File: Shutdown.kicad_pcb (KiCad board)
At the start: 4 copper layers, 93.5 x 70 mm, 218 parts, among them IC1 MCP1804T-C002I/OT, J1 DRC23-24PA, J2 0430450629, Q1 SI2347DS-T1-GE3, Q10 SI2318CDS-T1-GE3, Q11 SI2347DS-T1-GE3, Q12 SI2347DS-T1-GE3, Q13 SI2347DS-T1-GE3, Q14 MMBT3904L RFG, Q15 SI2347DS-T1-GE3, Q16 SI2347DS-T1-GE3, Q17 MMBT3904L RFG, Q18 SI2318CDS-T1-GE3, Q19 SI2318CDS-T1-GE3, Q2 SI2347DS-T1-GE3, Q20 SI2347DS-T1-GE3, Q21 SI2347DS-T1-GE3, Q22 SI2347DS-T1-GE3, Q23 SI2318CDS-T1-GE3, Q3 SI2318CDS-T1-GE3, Q4 SI2347DS-T1-GE3, Q5 SI2318CDS-T1-GE3, Q6 SI2347DS-T1-GE3, Q7 SI2347DS-T1-GE3, Q8 SI2347DS-T1-GE3, Q9 SI2318CDS-T1-GE3, U1 LM393BIDR, U2 LM393BIDR, U4 LM393BIDR, U5 CD4002BM96, U6 LM393BIDR

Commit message: test push
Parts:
- removed ? (x4): , 
- removed J1: DRC23-24PA, -Connectors:DRC2324PB
- removed J2: 0430450629, -Connectors:CONN_SD-43045-010_06_MOL
- removed R95: 100k, Resistor_SMD:R_0603_1608Metric_Pad0.98x0.95mm_HandSolder
- added C12: 100nF, Capacitor_SMD:C_0603_1608Metric_Pad1.08x0.95mm_HandSolder, F.Cu at (345.9, 132.9)
- added C13: 100nF, Capacitor_SMD:C_0603_1608Metric_Pad1.08x0.95mm_HandSolder, F.Cu at (345.9, 135.4)
- added J3: 348302001, -Connectors:348302001, F.Cu at (170.4, 188.4)
- added J4: 348300801, -Connectors:348300801, F.Cu at (227.0, 188.4)
- added R60: 510, Resistor_SMD:R_0603_1608Metric_Pad0.98x0.95mm_HandSolder, F.Cu at (387.2, 131.2)
- added U3: LM393BIDR, Package_SO:SOIC-8_3.9x4.9mm_P1.27mm, F.Cu at (395.4, 55.1)
- added U7: TSB712AIDT, Package_SO:SOIC-8_5.3x5.3mm_P1.27mm, F.Cu at (338.6, 142.0)
- C1: value 470nF -> 10uF
- C2: value 100nF -> 10uF
- C3: value 1uF -> 470nF
- C4, C5: value 100nF -> 1uF
- C8: value 1uF -> 100nF
- D1, D10, D11, D12, D28, D6, D7, D8: value Red -> BZT52C16; footprint LED_SMD:LED_0805_2012Metric -> Diode_SMD:D_SOD-123
- D13, D19, D2, D21, D23, D3, D4, D41, D42, D45, D5: value BZT52C16 -> Red; footprint Diode_SMD:D_SOD-123 -> LED_SMD:LED_0805_2012Metric
- D17: value BZT52C16 -> Red; footprint Diode_SMD:D_SOD-123 -> LED_SMD:LED_0805_2012Metric; moved to F.Cu
- D27, D32, D33, D35, D36, D38, D39, D44, Q20, R64, R66, R70, R72, R93, TP17, TP20, TP21, TP22, TP23, TP25: moved to F.Cu
- D30, D31, D34, D37: value Red -> BZT52C16; footprint LED_SMD:LED_0805_2012Metric -> Diode_SMD:D_SOD-123; moved to F.Cu
- Q10: value SI2318CDS-T1-GE3 -> MMBT3904L RFG
- Q11: value SI2347DS-T1-GE3 -> MMBT3904L RFG
- Q13, Q15, Q2, Q7: value SI2347DS-T1-GE3 -> SI2318CDS-T1-GE3
- Q14: value MMBT3904L RFG -> SI2347DS-T1-GE3
- Q17: value MMBT3904L RFG -> SI2318CDS-T1-GE3
- Q18, Q19, Q23, Q9: value SI2318CDS-T1-GE3 -> SI2347DS-T1-GE3
- R1, R37, R38, R39: value 100k -> 10k
- R11: value 100k -> 2.2k
- R12: value 10k -> 100k; moved to F.Cu
- R13, R18, R30, R52: value 510 -> 100k
- R17: value 100k -> 390k
- R21, R22, R26, R27, R28, R3: value 100k -> 0
- R23, R25: value 510 -> 0
- R24: value 10k -> 0
- R29: value 10k -> 100k
- R31: value 1k -> 100k
- R32: value 2.2k -> 100k
- R35: value 100k -> 1k
- R36: value 0 -> 1k
- R4, R5, R58, R6, R77, R78, R81, R82, R94: value 100k -> 510
- R40, R41, R42: value 510 -> 10k
- R43: value 1k -> 3M
- R44: value 10k -> 30k
- R45: value 10k -> 120k
- R47: value 510 -> 3k
- R53, R54: value 10k -> 510
- R55: value 3k -> 100k
- R56: value 3M -> 100k
- R57, R63, R67, R68, R69: value 510 -> 100k; moved to F.Cu
- R59: value 100k -> 51
- R61: value 120k -> 100k
- R62: value 30k -> 100k
- R65, R71: value 510 -> 51; moved to F.Cu
- R7: value 390k -> 510
- R73, R74, R75: value 51 -> 100k
- R80: value 100k -> 1M
- R84, R87, R88, R91, R92: value 0 -> 100k; moved to F.Cu
- R85: value 100k -> 510; moved to F.Cu
- R86: value 0 -> 510
- R89, R90: value 0 -> 510; moved to F.Cu
- TP24: footprint TestPoint:TestPoint_Pad_1.5x1.5mm -> TestPoint:TestPoint_Pad_1.0x1.0mm; moved to F.Cu
- TP27: footprint TestPoint:TestPoint_Pad_1.5x1.5mm -> TestPoint:TestPoint_Pad_1.0x1.0mm
- TP7, TP8: footprint TestPoint:TestPoint_Pad_1.0x1.0mm -> TestPoint:TestPoint_Pad_1.5x1.5mm
- U6: value LM393BIDR -> TSB712AIDT; footprint Package_SO:SOIC-8_3.9x4.9mm_P1.27mm -> Package_SO:SOIC-8_5.3x5.3mm_P1.27mm
- moved R47 310.6 mm to (419.2, 39.8), turned to 0 degrees
- moved R42 308.7 mm to (414.9, 49.9), turned to 0 degrees
- moved D26 304.7 mm to (414.8, 119.1), turned to 0 degrees
- moved R41 301.7 mm to (414.9, 47.4), turned to 0 degrees
- moved D28 301.0 mm to (414.8, 122.5), turned to 0 degrees
- moved TP23 300.0 mm to (408.6, 77.2), turned to 0 degrees
- moved R31 299.9 mm to (410.6, 44.9)
- moved TP22 299.7 mm to (408.6, 73.6), turned to 0 degrees
- moved TP21 299.5 mm to (408.6, 70.0), turned to 0 degrees
- moved Q16 298.6 mm to (409.3, 119.8)
- moved TP6 296.1 mm to (417.0, 79.0)
- moved TP8 295.8 mm to (401.4, 66.5)
- moved R40 294.8 mm to (414.9, 44.9), turned to 0 degrees
- moved D44 294.7 mm to (410.0, 95.1), turned to 0 degrees
- moved R29 292.9 mm to (410.6, 39.8), turned to 0 degrees
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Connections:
- C1 pad 2: Net-(C1-Pad2) -> /ISENSE-EXT
- C10 pad 2: /ACCUM-VOUT -> 12V
- C11 pad 2: Net-(U6A--) -> 12V
- C2 pad 2: 12V -> /BSE
- C3 pad 2: BATT+PROT -> Net-(C3-Pad2)
- C4 pad 2: 12V -> BATT+PROT
- C6 pad 2: 12V -> Net-(U4A--)
- C9 pad 2: /BRAKE-VOUT -> 12V
- D1 pad 1: GND -> Net-(D1-K)
- D10 pad 1: Net-(D10-K) -> /IMD-Fault-Passthru/OUTPUT
- D11 pad 1: GND -> Net-(D11-K)
- D11 pad 2: Net-(D11-A) -> GND
- D12 pad 1: Net-(D12-K) -> 12V
- D13 pad 1: /BMS-Fault-Passthru/OUTPUT -> GND
- D15 pad 1: Net-(D15-K) -> 12V
- D16 pad 1: Net-(D16-K) -> GND
- D17 pad 1: Net-(D17-K) -> GND
- D18 pad 1: Net-(D18-K) -> /BMS-Fault-Passthru/INPUT
- D18 pad 2: GND -> Net-(D18-A)
- D19 pad 1: /IMD-Fault-Passthru/OUTPUT -> Net-(D19-K)
- D2 pad 1: /HVILS-A -> GND
- D20 pad 2: GND -> Net-(D20-A)
- D21 pad 1: BATT+PROT -> Net-(D19-K)
- D22 pad 1: Net-(D22-K) -> BATT+PROT
- D22 pad 2: GND -> Net-(D22-A)
- D23 pad 1: /CS-A -> Net-(D23-K)
- D24 pad 1: /BOTS-A -> Net-(D24-K)
- D25 pad 1: GND -> Net-(D23-K)
- D26 pad 1: /BOTS-B -> /BMS-Fault-Passthru/OUTPUT
- D27 pad 1: /BYPASS -> Net-(D27-K)
- D28 pad 1: GND -> Net-(D28-K)
- D29 pad 1: GND -> Net-(D27-K)
- D3 pad 1: BATT+PROT -> GND
- D30 pad 1: GND -> BATT+PROT
- D31 pad 1: GND -> Net-(D31-K)
- D34 pad 1: GND -> /HVILS-A
- D35 pad 1: Net-(D10-K) -> GND
- D36 pad 1: Net-(D12-K) -> GND
- D37 pad 1: Net-(D16-K) -> /CRASH-SW-A
- D4 pad 1: /BMS-Fault-Passthru/INPUT -> /BYPASS-BTN
- D40 pad 1: 12V -> /BOTS-A
- D41 pad 1: 12V -> GND
- D42 pad 1: Net-(D42-K) -> GND
- D43 pad 1: BATT+PROT -> /BOTS-B
- D45 pad 1: Net-(D45-K) -> GND
- D45 pad 2: GND -> Net-(D45-A)
- D5 pad 1: Net-(D5-K) -> /BYPASS-BTN
- D6 pad 1: /BYPASS -> Net-(D6-K)
- D6 pad 2: Net-(D6-A) -> GND
- D7 pad 1: GND -> Net-(D7-K)
- D7 pad 2: Net-(D7-A) -> GND
- D8 pad 1: GND -> BATT+PROT
- D9 pad 2: Net-(D9-A) -> GND
- Q1 pad 1: Net-(D3-A) -> Net-(D1-A)
- Q1 pad 2: BATT+PROT -> Net-(D1-K)
- Q1 pad 3: /BMS-Fault-Passthru/INPUT -> BATT+
- Q10 pad 1: Net-(D15-K) -> Net-(Q10-B)
- Q10 pad 2: Net-(D15-A) -> Net-(Q10-E)
- Q10 pad 3: Net-(D16-K) -> /BSPD-FAULT-VCU
- Q11 pad 1: Net-(D40-A) -> Net-(Q11-B)
- Q11 pad 2: 12V -> GND
- Q11 pad 3: Net-(Q11-D) -> Net-(Q10-E)
- Q12 pad 1: Net-(D41-A) -> Net-(D18-A)
- Q12 pad 2: 12V -> /BMS-Fault-Passthru/INPUT
- Q12 pad 3: Net-(Q12-D) -> /BMS-Fault-Passthru/OUTPUT
- Q13 pad 1: Net-(D24-A) -> Net-(D20-K)
- Q13 pad 2: /BOTS-A -> Net-(D20-A)
- Q13 pad 3: Net-(Q13-D) -> Net-(D19-K)
- Q14 pad 1: Net-(Q14-B) -> Net-(D22-A)
- Q14 pad 2: Net-(Q14-E) -> BATT+PROT
- Q14 pad 3: /BSPD-FAULT -> /BMS-Fault-Passthru/INPUT
- Q15 pad 1: Net-(D2-A) -> Net-(D24-K)
- Q15 pad 2: /HVILS-A -> Net-(D24-A)
- Q15 pad 3: Net-(Q15-D) -> Net-(D23-K)
- Q16 pad 2: /BOTS-B -> /BMS-Fault-Passthru/OUTPUT
- Q16 pad 3: Net-(Q16-D) -> /IMD-Fault-Passthru/OUTPUT
- Q17 pad 1: Net-(Q17-B) -> Net-(D28-K)
- Q17 pad 2: GND -> Net-(D28-A)
- Q17 pad 3: Net-(Q14-E) -> Net-(D27-K)
- Q18 pad 1: Net-(D18-K) -> Net-(D30-A)
- Q18 pad 2: GND -> BATT+PROT
- Q18 pad 3: /IMD-FAULT -> Net-(D31-K)
- Q19 pad 1: Net-(D22-K) -> Net-(D31-A)
- Q19 pad 2: GND -> Net-(D31-K)
- Q19 pad 3: /BYPASS -> /TSSI-STATUS
- Q2 pad 1: Net-(D4-A) -> Net-(D6-K)
- Q2 pad 2: /BMS-Fault-Passthru/INPUT -> GND
- Q2 pad 3: /BMS-Fault-Passthru/OUTPUT -> /BMS-FAULT-VCU
- Q20 pad 1: Net-(D17-A) -> Net-(D34-A)
- Q20 pad 2: Net-(D17-K) -> /HVILS-A
- Q20 pad 3: BATT+ -> Net-(Q20-D)
- Q21 pad 1: Net-(D42-A) -> Net-(D37-A)
- Q21 pad 2: Net-(D42-K) -> /CRASH-SW-A
- Q21 pad 3: /STATUS-LIGHT -> Net-(Q21-D)
- Q22 pad 1: Net-(D43-A) -> Net-(D40-A)
- Q22 pad 2: BATT+PROT -> /BOTS-A
- Q22 pad 3: Net-(D42-K) -> Net-(Q22-D)
- Q23 pad 1: Net-(D45-K) -> Net-(D43-A)
- Q23 pad 2: GND -> /BOTS-B
- Q23 pad 3: /BMS-FAULT -> Net-(Q23-D)
- Q3 pad 1: Net-(D5-K) -> Net-(D7-K)
- Q3 pad 2: Net-(D5-A) -> GND
- Q3 pad 3: Net-(D10-K) -> /IMD-FAULT-VCU
- Q4 pad 1: Net-(D19-A) -> Net-(D8-A)
- Q4 pad 2: /IMD-Fault-Passthru/OUTPUT -> BATT+PROT
- Q4 pad 3: /HVILS-A -> Net-(Q4-D)
- Q5 pad 1: Net-(D20-K) -> Net-(D9-K)
- Q5 pad 3: /BYPASS -> /BYPASS-BTN
- Q6 pad 1: Net-(D21-A) -> Net-(D10-A)
- Q6 pad 2: BATT+PROT -> /IMD-Fault-Passthru/OUTPUT
- Q6 pad 3: Net-(Q6-D) -> /HVILS-A
- Q7 pad 1: Net-(D13-A) -> Net-(D11-K)
- Q7 pad 2: /BMS-Fault-Passthru/OUTPUT -> GND
- Q7 pad 3: /IMD-Fault-Passthru/OUTPUT -> /BYPASS-BTN
- Q8 pad 1: Net-(D23-A) -> Net-(D12-A)
- Q8 pad 2: /CS-A -> 12V
- Q9 pad 1: Net-(D9-K) -> Net-(D15-A)
- Q9 pad 2: Net-(D9-A) -> 12V
- Q9 pad 3: Net-(D12-K) -> Net-(Q9-D)
- R1 pad 1: Net-(D21-A) -> GND
- R1 pad 2: Net-(C1-Pad2) -> Net-(D1-A)
- R10 pad 1: GND -> Net-(D7-K)
- R10 pad 2: /BRAKE-VOUT -> /IMD-FAULT
- R11 pad 1: /BMS-FAULT -> GND
- R11 pad 2: Net-(D4-A) -> /IMD-FAULT
- R12 pad 1: GND -> Net-(D8-A)
- R12 pad 2: Net-(D17-A) -> Net-(C3-Pad2)
- R13 pad 1: Net-(D10-A) -> Net-(Q4-D)
- R13 pad 2: BATT+PROT -> Net-(D9-K)
- R14 pad 1: GND -> Net-(Q4-D)
- R14 pad 2: /CS-A -> GND
- R15 pad 1: /IMD-FAULT -> /BYPASS-BTN
- R15 pad 2: Net-(D13-A) -> BATT+PROT
- R16 pad 1: /BYPASS -> /BYPASS-BTN
- R16 pad 2: Net-(D19-A) -> Net-(D10-A)
- R17 pad 1: /AIR-COIL+ -> Net-(C3-Pad2)
- R17 pad 2: Net-(D26-A) -> BATT+PROT
- R18 pad 1: Net-(D29-A) -> Net-(D11-K)
- R18 pad 2: BATT+ -> /HVILS-A
- R19 pad 1: /BOTS-B -> Net-(R19-Pad1)
- R19 pad 2: Net-(D24-A) -> 12V
- R2 pad 1: /BSPD-FAULT -> GND
- R2 pad 2: BATT+PROT -> Net-(D1-K)
- R20 pad 1: /BOTS-A -> Net-(R20-Pad1)
- R20 pad 2: Net-(D23-A) -> 12V
- R21 pad 1: GND -> Net-(R21-Pad1)
- R21 pad 2: /HVILS-A -> 12V
- R22 pad 1: /BSPD-FAULT -> GND
- R22 pad 2: Net-(D5-K) -> Net-(R21-Pad1)
- R23 pad 1: Net-(D8-A) -> Net-(R23-Pad1)
- R23 pad 2: Net-(Q15-D) -> Net-(U1A-+)
- R24 pad 2: 12V -> Net-(U2B-+)
- R25 pad 1: Net-(D12-A) -> Net-(R25-Pad1)
- R25 pad 2: BATT+PROT -> 12V
- R26 pad 1: /BMS-FAULT -> GND
- R26 pad 2: Net-(D9-K) -> Net-(R25-Pad1)
- R27 pad 1: /IMD-FAULT -> Net-(U1A-+)
- R27 pad 2: Net-(D15-K) -> Net-(R21-Pad1)
- R28 pad 1: GND -> Net-(R25-Pad1)
- R28 pad 2: /ACCUM-VOUT -> Net-(U2B-+)
- R3 pad 1: GND -> Net-(D1-K)
- R3 pad 2: /AIR-COIL+ -> BATT+PROT
- R30 pad 1: Net-(D16-A) -> GND
- R30 pad 2: BATT+PROT -> Net-(R30-Pad2)
- R31 pad 1: /BRAKE-VOUT -> Net-(R31-Pad1)
- R31 pad 2: Net-(U4A--) -> 12V
- R32 pad 2: /IMD-OUT -> Net-(R32-Pad2)
- R33 pad 1: Net-(D18-K) -> GND
- R33 pad 2: /IMD-OUT -> /ISENSE-EXT
- R34 pad 1: /BYPASS -> GND
- R34 pad 2: BATT+PROT -> /BSE
- R35 pad 1: Net-(Q6-D) -> /ISENSE-EXT
- R35 pad 2: GND -> Net-(U2A--)
- R36 pad 1: Net-(R36-Pad1) -> /BSE
- R36 pad 2: Net-(U1A-+) -> Net-(U3A--)
- R37 pad 1: Net-(Q6-D) -> Net-(R37-Pad1)
- R37 pad 2: Net-(D20-K) -> 12V
- R38 pad 1: Net-(D22-K) -> Net-(R38-Pad1)
- R38 pad 2: /HVILS-A -> 12V
- R39 pad 1: /CS-A -> Net-(R39-Pad1)
- R39 pad 2: Net-(D2-A) -> 12V
- R4 pad 1: GND -> Net-(D2-A)
- R4 pad 2: /BOTS-B -> BATT+
- R40 pad 1: Net-(D1-A) -> Net-(R40-Pad1)
- R40 pad 2: Net-(Q8-D) -> 12V
- R41 pad 1: Net-(D7-A) -> Net-(R41-Pad1)
- R41 pad 2: Net-(Q13-D) -> 12V
- R42 pad 1: Net-(D25-A) -> Net-(R42-Pad1)
- R42 pad 2: Net-(Q16-D) -> 12V
- R43 pad 1: /ACCUM-VOUT -> Net-(R43-Pad1)
- R43 pad 2: Net-(U2A--) -> Net-(U4A--)
- R44 pad 1: Net-(R44-Pad1) -> Net-(U4A-+)
- R45 pad 1: Net-(R45-Pad1) -> GND
- R45 pad 2: 12V -> Net-(U4A-+)
- R46 pad 2: Net-(Q14-B) -> Net-(D12-A)
- R47 pad 1: Net-(D28-A) -> Net-(R47-Pad1)
- R47 pad 2: /AIR-COIL+ -> 12V
- R48 pad 1: Net-(D6-A) -> Net-(D13-A)
- R48 pad 2: BATT+PROT -> Net-(Q8-D)
- R49 pad 1: Net-(D11-A) -> Net-(D14-A)
- R49 pad 2: Net-(Q11-D) -> Net-(Q8-D)
- R5 pad 1: GND -> Net-(D3-A)
- R5 pad 2: /BOTS-A -> BATT+
- R50 pad 1: Net-(R50-Pad1) -> Net-(R47-Pad1)
- R50 pad 2: Net-(Q17-B) -> Net-(D15-A)
- R51 pad 1: GND -> Net-(R47-Pad1)
- R51 pad 2: /STATUS-LIGHT -> Net-(Q10-B)
- R52 pad 1: Net-(D14-A) -> Net-(R46-Pad1)
- R52 pad 2: Net-(Q12-D) -> Net-(Q11-B)
- R53 pad 1: Net-(R53-Pad1) -> Net-(D16-A)
- R53 pad 2: 12V -> Net-(Q9-D)
- R54 pad 1: Net-(R54-Pad1) -> Net-(D17-A)
- R54 pad 2: 12V -> Net-(Q9-D)
- R55 pad 1: Net-(R46-Pad1) -> /BMS-FAULT-VCU
- R55 pad 2: 12V -> BATT+PROT
- R56 pad 1: Net-(R56-Pad1) -> /BMS-FAULT-VCU
- R56 pad 2: Net-(U6A--) -> Net-(D18-A)
- R57 pad 1: Net-(D27-A) -> /BMS-FAULT-VCU
- R57 pad 2: BATT+PROT -> Net-(D20-K)
- R58 pad 1: Net-(R58-Pad1) -> Net-(D19-A)
- R58 pad 2: 12V -> BATT+PROT
- R59 pad 1: Net-(R59-Pad1) -> GND
- R59 pad 2: 12V -> Net-(D20-A)
- R6 pad 1: /BMS-FAULT -> Net-(D4-A)
- R61 pad 1: GND -> /BSPD-FAULT-VCU
- R61 pad 2: Net-(U6A-+) -> BATT+PROT
- R62 pad 1: Net-(U6A-+) -> /BSPD-FAULT-VCU
- R62 pad 2: 12V -> Net-(D22-A)
- R63 pad 1: Net-(D30-A) -> /BSPD-FAULT-VCU
- R63 pad 2: /AIR-COIL+ -> Net-(D24-K)
- R64 pad 1: Net-(D31-A) -> Net-(D23-A)
- R64 pad 2: Net-(Q16-D) -> BATT+PROT
- R65 pad 1: Net-(D32-A) -> GND
- R65 pad 2: Net-(Q13-D) -> Net-(D24-A)
- R66 pad 1: Net-(D33-A) -> Net-(D25-A)
- R66 pad 2: Net-(Q8-D) -> BATT+PROT
- R67 pad 1: Net-(D34-A) -> /IMD-FAULT-VCU
- R67 pad 2: Net-(Q15-D) -> BATT+PROT
- R68 pad 1: Net-(D35-A) -> /IMD-FAULT-VCU
- R68 pad 2: BATT+PROT -> Net-(D26-A)
- R69 pad 1: Net-(D36-A) -> /IMD-FAULT-VCU
- R69 pad 2: BATT+PROT -> Net-(D28-K)
- R7 pad 1: Net-(C1-Pad2) -> Net-(D5-A)
- R70 pad 1: Net-(D37-A) -> Net-(D27-A)
- R71 pad 1: Net-(D38-A) -> GND
- R71 pad 2: Net-(Q12-D) -> Net-(D28-A)
- R72 pad 1: Net-(D39-A) -> Net-(D29-A)
- R72 pad 2: Net-(Q11-D) -> BATT+PROT
- R73 pad 1: GND -> /IMD-FAULT-VCU
- R73 pad 2: Net-(D5-A) -> Net-(D30-A)
- R74 pad 1: GND -> /BMS-FAULT-VCU
- R74 pad 2: Net-(D9-A) -> Net-(D31-A)
- R75 pad 2: Net-(D15-A) -> /TSSI-STATUS
- R76 pad 1: Net-(R46-Pad1) -> GND
- R76 pad 2: Net-(D41-A) -> /HVILS-A
- R77 pad 1: Net-(R50-Pad1) -> Net-(D32-A)
- R77 pad 2: Net-(D40-A) -> Net-(Q20-D)
- R78 pad 1: /BMS-FAULT -> Net-(D33-A)
- R78 pad 2: Net-(D42-A) -> Net-(Q20-D)
- R79 pad 1: /IMD-FAULT -> /CRASH-SW-A
- R79 pad 2: Net-(D43-A) -> Net-(D34-A)
- R8 pad 1: /IMD-FAULT -> Net-(D6-K)
- R8 pad 2: BATT+PROT -> /BMS-FAULT
- R80 pad 1: Net-(R80-Pad1) -> GND
- R80 pad 2: 12V -> /CRASH-SW-A
- R81 pad 1: GND -> Net-(D35-A)
- R81 pad 2: Net-(R81-Pad2) -> Net-(Q21-D)
- R82 pad 1: Net-(R82-Pad1) -> Net-(D36-A)
- R82 pad 2: 12V -> Net-(Q21-D)
- R83 pad 1: GND -> /BOTS-A
- R83 pad 2: Net-(R83-Pad2) -> Net-(D37-A)
- R84 pad 1: Net-(D17-K) -> GND
- R84 pad 2: BATT+PROT -> /BOTS-A
- R85 pad 1: GND -> Net-(D38-A)
- R85 pad 2: Net-(D17-K) -> Net-(Q22-D)
- R86 pad 1: Net-(R86-Pad1) -> Net-(D39-A)
- R86 pad 2: Net-(U1B-+) -> Net-(Q22-D)
- R87 pad 1: Net-(R87-Pad1) -> /BOTS-B
- R87 pad 2: 12V -> Net-(D40-A)
- R88 pad 2: Net-(R87-Pad1) -> /BOTS-B
- R89 pad 1: Net-(U1A-+) -> Net-(D41-A)
- R89 pad 2: Net-(R87-Pad1) -> Net-(Q23-D)
- R9 pad 1: /BSPD-FAULT -> GND
- R9 pad 2: Net-(D3-A) -> /BMS-FAULT
- R90 pad 1: GND -> Net-(D42-A)
- R90 pad 2: Net-(R90-Pad2) -> Net-(Q23-D)
- R91 pad 1: Net-(R90-Pad2) -> /SD-POWER
- R91 pad 2: Net-(U1B-+) -> Net-(D43-A)
- R92 pad 1: Net-(R90-Pad2) -> GND
- R92 pad 2: 12V -> /SD-POWER
- R93 pad 2: BATT+ -> /SD-POWER
- R94 pad 1: Net-(D45-K) -> Net-(D45-A)
- R94 pad 2: /BMS-OUT -> /SD-POWER
- RV1 pad 1: Net-(R58-Pad1) -> Net-(R19-Pad1)
- RV1 pad 2: Net-(R36-Pad1) -> Net-(R23-Pad1)
- RV2 pad 1: Net-(R82-Pad1) -> Net-(R20-Pad1)
- RV2 pad 2: Net-(U4A-+) -> Net-(R24-Pad1)
- RV3 pad 1: 12V -> Net-(R29-Pad1)
- RV3 pad 2: Net-(U4B--) -> Net-(U2A-+)
- RV3 pad 3: Net-(R83-Pad2) -> GND
- RV4 pad 1: Net-(R59-Pad1) -> 12V
- RV4 pad 2: Net-(R86-Pad1) -> Net-(U3B--)
- RV4 pad 3: GND -> Net-(R30-Pad2)
- RV5 pad 1: Net-(R80-Pad1) -> Net-(R31-Pad1)
- RV5 pad 2: Net-(U2A-+) -> Net-(U3A-+)
- RV6 pad 2: Net-(U2B--) -> Net-(U4B--)
- RV6 pad 3: Net-(R81-Pad2) -> Net-(R32-Pad2)
- TP1 pad 1: /BMS-Fault-Passthru/INPUT -> Net-(D1-K)
- TP10 pad 1: Net-(U4A-+) -> Net-(U3B--)
- TP11 pad 1: Net-(U4B--) -> Net-(U3A-+)
- TP12 pad 1: Net-(U1B-+) -> Net-(U4B--)
- TP13 pad 1: Net-(R54-Pad1) -> Net-(U1A-+)
- TP14 pad 1: Net-(U2A-+) -> Net-(U2B-+)
- TP15 pad 1: Net-(U2B--) -> Net-(U2A-+)
- TP16 pad 1: Net-(R53-Pad1) -> Net-(U3B--)
- TP17 pad 1: Net-(U1A-+) -> Net-(U3A-+)
- TP18 pad 1: Net-(R50-Pad1) -> Net-(U4B--)
- TP19 pad 1: Net-(R46-Pad1) -> Net-(R38-Pad1)
- TP2 pad 1: /BMS-Fault-Passthru/OUTPUT -> /BMS-Fault-Passthru/INPUT
- TP20 pad 1: Net-(U1B-+) -> Net-(R37-Pad1)
- TP21 pad 1: Net-(U2A-+) -> Net-(R46-Pad1)
- TP22 pad 1: Net-(U2B--) -> Net-(R47-Pad1)
- TP23 pad 1: Net-(U4A-+) -> /BSPD-FAULT-VCU
- TP24 pad 1: Net-(U4B--) -> /CRASH-SW-A
- TP25 pad 1: Net-(D17-K) -> /BOTS-A
- TP26 pad 1: 12V -> /BOTS-B
- TP27 pad 1: /BSPD-FAULT -> /SD-POWER
- TP3 pad 1: /IMD-Fault-Passthru/OUTPUT -> /BMS-Fault-Passthru/OUTPUT
- TP4 pad 1: /HVILS-A -> /IMD-Fault-Passthru/OUTPUT
- TP5 pad 1: /CS-A -> /HVILS-A
- TP6 pad 1: /BOTS-A -> 12V
- TP7 pad 1: /BOTS-B -> Net-(U1A-+)
- TP8 pad 1: /AIR-COIL+ -> Net-(U2B-+)
- TP9 pad 1: Net-(U1A-+) -> Net-(U2A-+)
- U1 pad 1: Net-(R54-Pad1) -> Net-(R37-Pad1)
- U1 pad 2: /ACCUM-VOUT -> /ISENSE-EXT
- U1 pad 5: Net-(U1B-+) -> GND
- U1 pad 6: /BRAKE-VOUT -> Net-(U1B--)
- U1 pad 7: Net-(R53-Pad1) -> Net-(U1B--)
- U2 pad 1: Net-(R45-Pad1) -> Net-(R39-Pad1)
- U2 pad 5: Net-(U2A--) -> Net-(U2B-+)
- U2 pad 6: Net-(U2B--) -> /BSE
- U2 pad 7: Net-(R44-Pad1) -> Net-(R38-Pad1)
- U4 pad 1: Net-(R29-Pad1) -> Net-(R47-Pad1)
- U4 pad 5: Net-(U4A--) -> Net-(U3A--)
- U4 pad 7: Net-(R24-Pad1) -> Net-(R42-Pad1)
- U5 pad 1: Net-(R56-Pad1) -> Net-(R43-Pad1)
- U5 pad 10: Net-(R44-Pad1) -> Net-(R40-Pad1)
- U5 pad 11: Net-(R29-Pad1) -> Net-(R41-Pad1)
- U5 pad 12: Net-(R24-Pad1) -> Net-(R42-Pad1)
- U5 pad 13: Net-(R50-Pad1) -> Net-(R46-Pad1)
- U5 pad 2: Net-(R54-Pad1) -> Net-(R37-Pad1)
- U5 pad 3: Net-(R54-Pad1) -> Net-(R37-Pad1)
- U5 pad 4: Net-(R53-Pad1) -> Net-(R38-Pad1)
- U5 pad 5: Net-(R53-Pad1) -> Net-(R38-Pad1)
- U5 pad 9: Net-(R45-Pad1) -> Net-(R39-Pad1)
- U6 pad 1: Net-(R46-Pad1) -> /BSPD-FAULT-VCU-BUF
- U6 pad 2: Net-(U6A--) -> /BSPD-FAULT-VCU-BUF
- U6 pad 3: Net-(U6A-+) -> /BSPD-FAULT-VCU
- U6 pad 5: unconnected-(U6B-+-Pad5) -> /BMS-FAULT-VCU
- U6 pad 6: unconnected-(U6B---Pad6) -> /BMS-FAULT-VCU-BUF
- U6 pad 7: unconnected-(U6-Pad7) -> /BMS-FAULT-VCU-BUF
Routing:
- net GND: track 437.3 -> 0.00 mm, vias 17 -> 0
- net BATT+PROT: track 177.4 -> 0.00 mm, vias 12 -> 0
- net /HVILS-A: track 145.2 -> 0.00 mm
- net /BOTS-B: track 143.9 -> 0.00 mm
- net /AIR-COIL+: track 143.2 -> 0.00 mm
- net 12V: track 124.7 -> 0.00 mm, vias 9 -> 0
- net /BRAKE-VOUT: track 90.2 -> 0.00 mm, vias 3 -> 0
- net /IMD-FAULT: track 89.5 -> 0.00 mm, vias 1 -> 0
- net /BMS-FAULT: track 85.1 -> 0.00 mm, vias 2 -> 0
- net /STATUS-LIGHT: track 83.0 -> 0.00 mm
- net /BSPD-FAULT: track 75.7 -> 0.00 mm, vias 3 -> 0
- net /BOTS-A: track 73.8 -> 0.00 mm
- net /ACCUM-VOUT: track 73.1 -> 0.00 mm, vias 2 -> 0
- net /CS-A: track 65.2 -> 0.00 mm
- net /BMS-OUT: track 57.3 -> 0.00 mm, vias 2 -> 0
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- removed copper zone on In2.Cu, net 12V
- removed copper zone on In2.Cu, net BATT+PROT
- removed copper zone on In1.Cu, net GND
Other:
- board size 93.5 x 70 mm -> 152.4 x 112.4 mm
- board text removed: "12V"
- board text removed: "12V_R"
- board text removed: "BMS"
- board text removed: "BOTS"
- board text removed: "BRK 12V SHORT"
- board text removed: "BRK GND SHORT"
- board text removed: "BSPD"
- board text removed: "BSPD OUT"
- board text removed: "Board Jump"
- board text removed: "Board Power"
- board text removed: "Brake Thres"
- board text removed: "Brake Threshold"
- board text removed: "Brake to 12V SHORT"
- board text removed: "Brake to GND SHORT"
- board text removed: "Brk State (LOW=BRAKING)"
- board text removed: "Brk Thres"
- board text removed: "Bypass"
- board text removed: "CRASH SWITCH"
- board text removed: "CS"
- board text removed: "Curr. Thres"
- board text removed: "Current Threshold"
- board text removed: "HVILS"
- board text removed: "HVILs"
- board text removed: "IMD"
- board text removed: "IMPLAUS."
- board text removed: "INVALID"
- board text removed: "I_S 12V SHORT"
- board text removed: "I_S GND SHORT"
- board text removed: "I_S State (LOW=CURRENT)"
- board text removed: "I_S Thres"
- board text removed: "I_S to 12V SHORT"
- board text removed: "I_S to GND SHORT"
- board text removed: "Latch"
- board text removed: "Mk11 Shutdown V1"
- board text removed: "Prot12V"
- board text removed: "SD OK"
- board text removed: "SIGNAL"
- board text removed: "SYSTEM"
- board text removed: "Signal Invalid"
- board text removed: "System Plaus."
- board text removed: "TSMS"
- board text removed: "Test Load"

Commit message: completed placement:
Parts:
- removed IC1: MCP1804T-C002I/OT, -LDO:SOT95P270X145-5N
- removed the TP13 at (405.0, 63.0)
- removed the TP14 at (405.0, 66.5)
- removed the TP15 at (405.0, 70.0)
- removed TP16, TP18: ~, TestPoint:TestPoint_Pad_1.5x1.5mm
- removed the TP17 at (405.0, 77.2)
- removed the U2 at (395.4, 48.5)
- added MH1: ~, MountingHole:MountingHole_3.5mm_Pad_TopBottom, F.Cu at (151.7, 109.0)
- added MH2: ~, MountingHole:MountingHole_3.5mm_Pad_TopBottom, F.Cu at (248.0, 109.0)
- added MH3: ~, MountingHole:MountingHole_3.5mm_Pad_TopBottom, F.Cu at (265.2, 143.6)
- added MH4: ~, MountingHole:MountingHole_3.5mm_Pad_TopBottom, F.Cu at (151.7, 143.6)
- added U1: LM393BIDR, Package_SO:SOIC-8_3.9x4.9mm_P1.27mm, F.Cu at (214.1, 136.0)
- added U5: LM393BIDR, Package_SO:SOIC-8_3.9x4.9mm_P1.27mm, F.Cu at (249.3, 129.3)
- U3: value LM393BIDR -> MCP1804T-C002I/OT; footprint Package_SO:SOIC-8_3.9x4.9mm_P1.27mm -> Package_TO_SOT_SMD:SOT-23-5
- moved D36 258.9 mm to (152.9, 125.6), turned to 90 degrees
- moved D44 257.7 mm to (157.6, 141.3), turned to -90 degrees
- moved D37 255.7 mm to (155.7, 125.6), turned to 90 degrees
- moved D45 254.2 mm to (160.6, 141.3), turned to -90 degrees
- moved R76 249.9 mm to (152.9, 121.8), turned to 90 degrees
- moved D43 249.4 mm to (161.7, 110.3), turned to 90 degrees
- moved R94 247.8 mm to (160.6, 145.1), turned to -90 degrees
- moved D42 246.9 mm to (158.9, 110.3), turned to 90 degrees
- moved R77 246.8 mm to (155.7, 121.8), turned to 90 degrees
- moved R93 243.2 mm to (157.6, 145.1), turned to -90 degrees
- moved R82 241.7 mm to (163.5, 133.0), turned to 90 degrees
- moved TP26 239.7 mm to (158.5, 127.2)
- moved R85 239.7 mm to (158.2, 121.8), turned to 90 degrees
- moved R86 239.3 mm to (165.5, 133.0), turned to -90 degrees
- moved R91 238.4 mm to (158.9, 106.3), turned to 90 degrees
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- renumbered C7 to C4, C8 to C5, C4 to C6, C5 to C7, C6 to C8, D2 to D1, D11 to D10, D8 to D11, D15 to D12, D16 to D13, D17 to D14, D12 to D15, D13 to D16, D14 to D17, D3 to D2, D21 to D20, D20 to D21, D25 to D24, D24 to D25, D29 to D28, D28 to D29, D4 to D3, D34 to D32, D37 to D33, D40 to D34, D43 to D35, D44 to D36, D45 to D37, D32 to D38, D33 to D39, D5 to D4, D35 to D40, D36 to D41, D38 to D42, D39 to D43, D41 to D44, D42 to D45, D1 to D5, D10 to D6, D6 to D7, D7 to D8, J3 to J1, J4 to J2, Q8 to Q10, Q6 to Q2, Q2 to Q3, Q3 to Q4, Q7 to Q6, Q4 to Q7, Q9 to Q8, Q10 to Q9, R3 to R1, R16 to R10, R8 to R11, R10 to R12, R9 to R13, R11 to R14, R13 to R15, R14 to R16, R12 to R17, R17 to R18, R21 to R19, R4 to R2, R22 to R20, R19 to R21, R27 to R22, R44 to R23, R23 to R24, R37 to R25, R45 to R26, R47 to R27, R50 to R28, R43 to R29, R5 to R3, R20 to R30, R53 to R31, R54 to R32, R24 to R33, R38 to R34, R28 to R35, R25 to R36, R26 to R37, R29 to R38, R51 to R39, R6 to R4, R39 to R40, R35 to R41, R48 to R42, R49 to R43, R33 to R44, R52 to R45, R40 to R46, R46 to R47, R30 to R48, R31 to R49, R7 to R5, R41 to R50, R36 to R51, R34 to R52, R42 to R53, R32 to R54, R58 to R55, R60 to R56, R55 to R57, R56 to R58, R57 to R59, R2 to R6, R59 to R60, R64 to R61, R66 to R62, R61 to R63, R62 to R64, R63 to R65, R65 to R66, R70 to R67, R72 to R68, R67 to R69, R1 to R7, R68 to R70, R69 to R71, R71 to R72, R93 to R76, R94 to R77, R76 to R78, R18 to R8, R83 to R80, R87 to R81, R91 to R82, R80 to R83, R88 to R85, R92 to R86, R77 to R87, R78 to R88, R81 to R89, R15 to R9, R82 to R90, R85 to R91, R86 to R92, R89 to R93, R90 to R94, TP22 to TP10, TP8 to TP11, TP19 to TP13, TP23 to TP14, TP9 to TP15, TP10 to TP17, TP21 to TP19, TP11 to TP20, TP12 to TP22, TP7 to TP6, TP20 to TP8, TP6 to TP9, U1 to U2, U5 to U4, U4 to U6, U6 to U7, U7 to U8
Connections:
- C8 pad 2: Net-(U4A--) -> Net-(U2A--)
- J2 pad 1: /SD-POWER -> BATT+
- J2 pad 2: /SD-POWER -> BATT+
- J2 pad 3: /SD-POWER -> GND
- J2 pad 5: BATT+ -> /SD-POWER
- J2 pad 6: BATT+ -> /SD-POWER
- J2 pad 7: GND -> /SD-POWER
- R23 pad 1: Net-(U4A-+) -> Net-(U2A-+)
- R25 pad 1: Net-(R37-Pad1) -> Net-(R25-Pad1)
- R26 pad 2: Net-(U4A-+) -> Net-(U2A-+)
- R27 pad 1: Net-(R47-Pad1) -> Net-(R27-Pad1)
- R28 pad 1: Net-(R47-Pad1) -> Net-(R27-Pad1)
- R29 pad 2: Net-(U4A--) -> Net-(U2A--)
- R39 pad 1: Net-(R47-Pad1) -> Net-(R27-Pad1)
- R41 pad 2: Net-(U2A--) -> Net-(U5A--)
- R46 pad 1: Net-(R40-Pad1) (its old number) -> Net-(R46-Pad1)
- R50 pad 1: Net-(R41-Pad1) -> Net-(R50-Pad1)
- R51 pad 2: Net-(U3A--) -> Net-(U6A--)
- RV4 pad 2: Net-(U3B--) -> Net-(U5B--)
- RV5 pad 2: Net-(U3A-+) -> Net-(U6A-+)
- TP10 pad 1: Net-(R47-Pad1) -> Net-(R27-Pad1)
- TP17 pad 1: Net-(U3B--) -> Net-(U5B--)
- TP20 pad 1: Net-(U3A-+) -> Net-(U6A-+)
- TP8 pad 1: Net-(R37-Pad1) -> Net-(R25-Pad1)
- U2 pad 1: Net-(R37-Pad1) -> Net-(R27-Pad1)
- U2 pad 2: /ISENSE-EXT -> Net-(U2A--)
- U2 pad 3: Net-(U1A-+) -> Net-(U2A-+)
- U3 pad 1: Net-(R41-Pad1) -> BATT+PROT
- U3 pad 2: Net-(U3A--) -> GND
- U3 pad 3: Net-(U3A-+) -> unconnected-(U3-NC-Pad3)
- U3 pad 4: GND -> BATT+PROT
- U3 pad 5: Net-(U2A--) -> 12V
- U4 pad 10: Net-(R40-Pad1) (its old number) -> Net-(R46-Pad1)
- U4 pad 11: Net-(R41-Pad1) -> Net-(R50-Pad1)
- U4 pad 2: Net-(R37-Pad1) -> Net-(R25-Pad1)
- U4 pad 3: Net-(R37-Pad1) -> Net-(R25-Pad1)
- U6 pad 1: Net-(R47-Pad1) -> Net-(R50-Pad1)
- U6 pad 2: Net-(U4A--) -> Net-(U6A--)
- U6 pad 3: Net-(U4A-+) -> Net-(U6A-+)
- U6 pad 5: Net-(U3A--) -> Net-(U6A--)
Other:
- board size 152.4 x 112.4 mm -> 127 x 61.3 mm

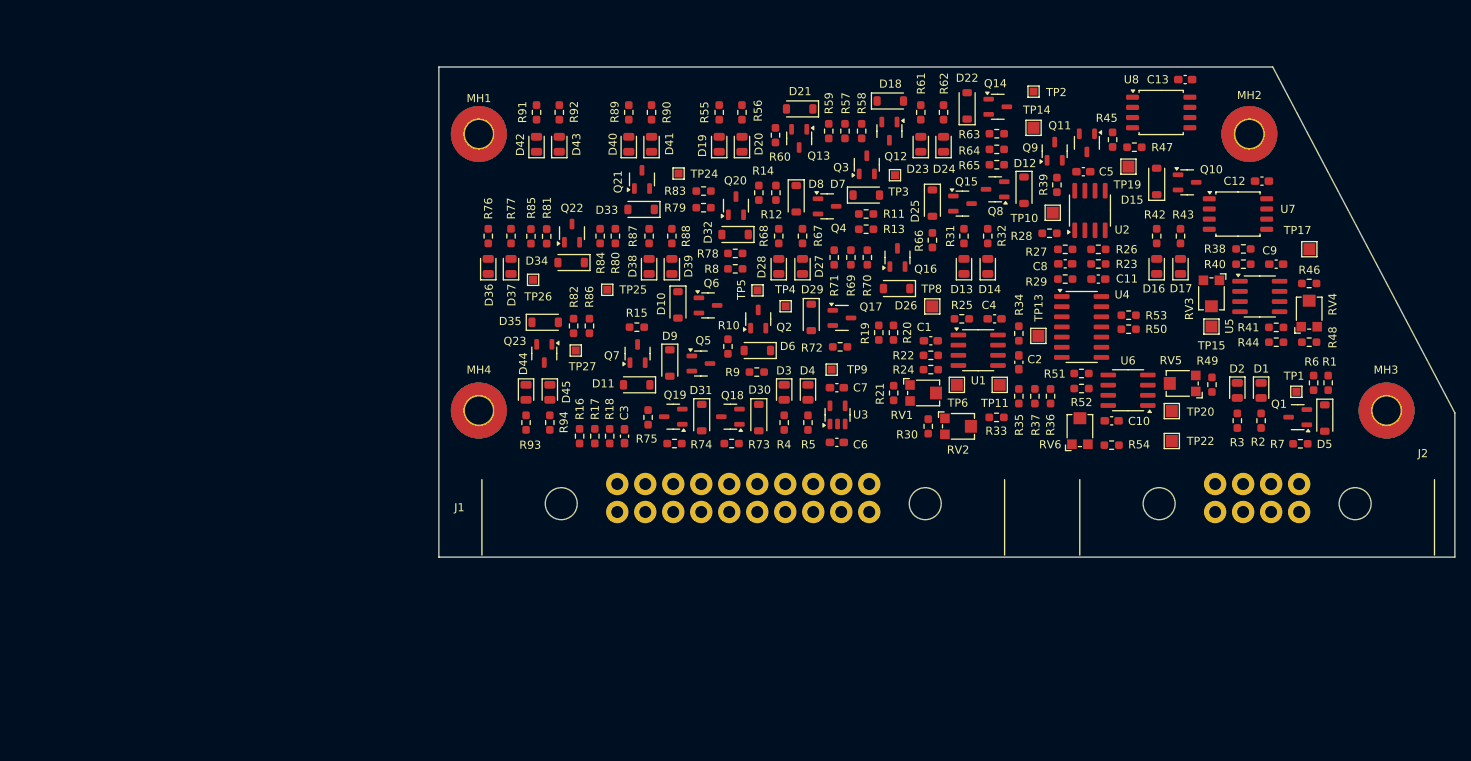
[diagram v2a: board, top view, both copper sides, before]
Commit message: changed BSPD, BMS fault logic to match Mk11 specs, all signals going back to VCU have 12V fault, 0V no fault readings, connector symbols/footprints left for next push
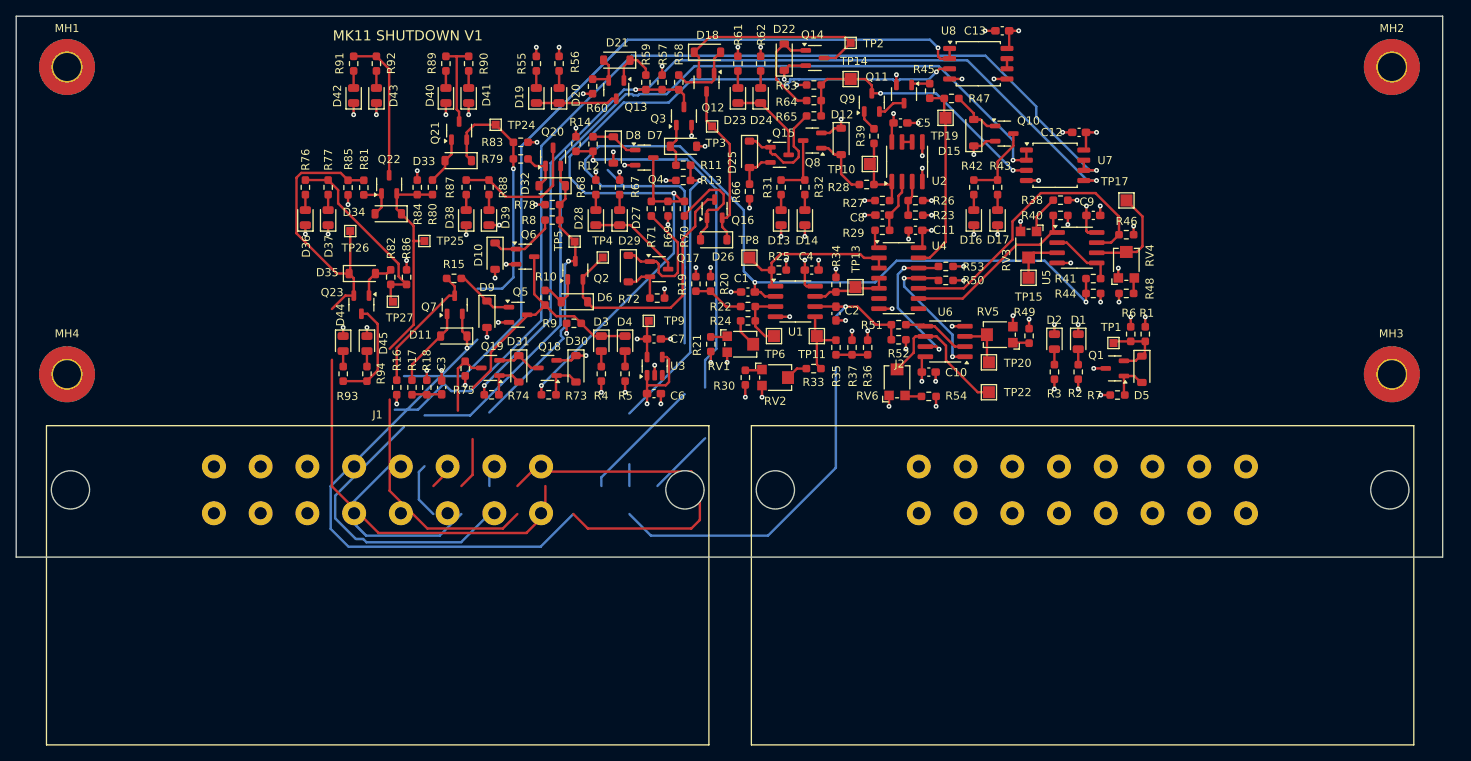
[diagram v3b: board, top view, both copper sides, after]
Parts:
- added G***: LOGO, LOGO, B.Cu at (203.1, 126.9)
- J1: value 348302001 -> 0194270049; footprint -Connectors:348302001 -> -Connectors:0194270049
- J2: value 348300801 -> 0194270049; footprint -Connectors:348300801 -> -Connectors:0194270049
- moved MH1 52.2 mm to (100.2, 100.6)
- moved MH4 51.7 mm to (100.2, 139.0)
- moved J1 45.7 mm to (139.0, 153.5)
- moved C10 23.7 mm to (207.9, 138.8)
- moved C3 23.7 mm to (147.0, 140.7)
- moved C8 23.7 mm to (202.1, 119.1)
- moved D1 23.7 mm to (226.6, 135.0)
- moved D11 23.7 mm to (148.6, 134.3)
- moved D12 23.7 mm to (197.0, 109.9)
- moved D18 23.7 mm to (180.3, 98.8)
- moved D2 23.7 mm to (223.6, 135.0)
- moved D3 23.7 mm to (167.0, 135.2)
- moved D30 23.7 mm to (163.8, 138.4)
- moved D31 23.7 mm to (156.7, 138.4)
- moved D33 23.7 mm to (149.1, 112.3)
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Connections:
- J1 pad 1: /TSSI-STATUS -> unconnected-(J1-Pad1)
- J1 pad 11: /BSPD-FAULT-VCU-BUF -> unconnected-(J1-Pad11)
- J1 pad 12: /BMS-FAULT-VCU-BUF -> unconnected-(J1-Pad12)
- J1 pad 13: /IMD-FAULT-VCU-BUF -> unconnected-(J1-Pad13)
- J1 pad 14: /BOTS-A -> unconnected-(J1-Pad14)
- J1 pad 15: /BOTS-B -> unconnected-(J1-Pad15)
- J1 pad 16: /CRASH-SW-A -> unconnected-(J1-Pad16)
- J1 pad 2: /BYPASS-BTN -> unconnected-(J1-Pad2)
- J1 pad 3: /HVILS-A -> unconnected-(J1-Pad3)
- J1 pad 4: /CRASH-SW-A -> unconnected-(J1-Pad4)
- J1 pad 5: /BOTS-B -> unconnected-(J1-Pad5)
- J1 pad 6: /SD-POWER -> unconnected-(J1-Pad6)
- J1 pad 7: /ISENSE-EXT -> unconnected-(J1-Pad7)
- J1 pad 8: /BMS-FAULT -> unconnected-(J1-Pad8)
- J1 pad 9: /IMD-FAULT -> unconnected-(J1-Pad9)
- J2 pad 1: BATT+ -> unconnected-(J2-Pad1)
- J2 pad 2: BATT+ -> unconnected-(J2-Pad2)
- J2 pad 3: GND -> unconnected-(J2-Pad3)
- J2 pad 4: GND -> unconnected-(J2-Pad4)
- J2 pad 5: /SD-POWER -> unconnected-(J2-Pad5)
- J2 pad 6: /SD-POWER -> unconnected-(J2-Pad6)
- J2 pad 7: /SD-POWER -> unconnected-(J2-Pad7)
- J2 pad 8: GND -> unconnected-(J2-Pad8)
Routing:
- net unconnected-(J1-Pad8): track 0.00 -> 147.2 mm
- net /BMS-FAULT-VCU-BUF: track 0.00 -> 129.1 mm, vias 0 -> 1
- net /ISENSE-EXT: track 0.00 -> 123.1 mm, vias 0 -> 2
- net /BMS-FAULT-VCU: track 0.00 -> 121.6 mm, vias 0 -> 3
- net /BSPD-FAULT-VCU-BUF: track 0.00 -> 120.2 mm, vias 0 -> 1
- net /IMD-FAULT-VCU: track 0.00 -> 113.0 mm, vias 0 -> 3
- net GND: track 0.00 -> 109.4 mm, vias 0 -> 73
- net /IMD-FAULT-VCU-BUF: track 0.00 -> 101.1 mm, vias 0 -> 1
- net unconnected-(J1-Pad16): track 0.00 -> 75.2 mm
- net 12V: track 0.00 -> 60.9 mm, vias 0 -> 26
- net /BOTS-A: track 0.00 -> 57.5 mm
- net /BSE: track 0.00 -> 57.1 mm, vias 0 -> 1
- net /IMD-FAULT: track 0.00 -> 54.1 mm, vias 0 -> 1
- net BATT+PROT: track 0.00 -> 39.2 mm, vias 0 -> 18
- net /BMS-FAULT: track 0.00 -> 38.6 mm, vias 0 -> 1
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- added copper zone on In1.Cu, net GND
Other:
- board size 127 x 61.3 mm -> 178.3 x 67.6 mm
- board text added: "MK11 SHUTDOWN V1"
- board text added: "MK11 Shutdown V1 Drive Documentation"

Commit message: update
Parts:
- removed C1, C2: 10uF, Capacitor_SMD:C_0603_1608Metric_Pad1.08x0.95mm_HandSolder
- removed C10, C11, C12, C13, C4, C5, C8, C9: 100nF, Capacitor_SMD:C_0603_1608Metric_Pad1.08x0.95mm_HandSolder
- removed C3: 470nF, Capacitor_SMD:C_0603_1608Metric_Pad1.08x0.95mm_HandSolder
- removed C6, C7: 1uF, Capacitor_SMD:C_0603_1608Metric_Pad1.08x0.95mm_HandSolder
- removed D1, D13, D14, D16, D17, D19, D2, D20, D23, D24, D27, D28, D3, D36, D37, D38, D39, D4, D40, D41, D42, D43, D44, D45: Red, LED_SMD:LED_0805_2012Metric
- removed D10, D11, D12, D15, D18, D21, D22, D25, D26, D29, D30, D31, D32, D33, D34, D35, D5, D6, D7, D8, D9: BZT52C16, Diode_SMD:D_SOD-123
- removed Q1, Q10, Q12, Q14, Q16, Q18, Q19, Q2, Q20, Q21, Q22, Q23, Q7, Q8: SI2347DS-T1-GE3, Package_TO_SOT_SMD:SOT-23-3
- removed Q11, Q9: MMBT3904L RFG, Package_TO_SOT_SMD:SOT-23-3
- removed Q13, Q15, Q17, Q3, Q4, Q5, Q6: SI2318CDS-T1-GE3, Package_TO_SOT_SMD:SOT-23-3
- removed R1, R19, R20, R22, R24, R33, R35, R36, R37: 0, Resistor_SMD:R_0603_1608Metric_Pad0.98x0.95mm_HandSolder
- removed R10, R11, R12, R13, R15, R16, R17, R21, R28, R30, R38, R39, R44, R45, R47, R48, R49, R52, R54, R57, R58, R59, R6, R63, R64, R65, R69, R70, R71, R73, R74, R75, R78, R79, R8, R80, R81, R82, R84, R85, R86, R9: 100k, Resistor_SMD:R_0603_1608Metric_Pad0.98x0.95mm_HandSolder
- removed R14: 2.2k, Resistor_SMD:R_0603_1608Metric_Pad0.98x0.95mm_HandSolder
- removed R18: 390k, Resistor_SMD:R_0603_1608Metric_Pad0.98x0.95mm_HandSolder
- removed R2, R3, R31, R32, R4, R42, R43, R5, R55, R56, R61, R62, R67, R68, R76, R77, R87, R88, R89, R90, R91, R92, R93, R94: 510, Resistor_SMD:R_0603_1608Metric_Pad0.98x0.95mm_HandSolder
- removed R23: 30k, Resistor_SMD:R_0603_1608Metric_Pad0.98x0.95mm_HandSolder
- removed R25, R34, R40, R46, R50, R53, R7: 10k, Resistor_SMD:R_0603_1608Metric_Pad0.98x0.95mm_HandSolder
- removed R26: 120k, Resistor_SMD:R_0603_1608Metric_Pad0.98x0.95mm_HandSolder
- removed R27: 3k, Resistor_SMD:R_0603_1608Metric_Pad0.98x0.95mm_HandSolder
- removed R29: 3M, Resistor_SMD:R_0603_1608Metric_Pad0.98x0.95mm_HandSolder
- removed R41, R51: 1k, Resistor_SMD:R_0603_1608Metric_Pad0.98x0.95mm_HandSolder
- removed R60, R66, R72: 51, Resistor_SMD:R_0603_1608Metric_Pad0.98x0.95mm_HandSolder
- removed R83: 1M, Resistor_SMD:R_0603_1608Metric_Pad0.98x0.95mm_HandSolder
- removed RV1, RV2, RV3, RV4, RV5, RV6: 100k, Potentiometer_SMD:Potentiometer_Bourns_TC33X_Vertical
- removed TP1, TP2, TP24, TP25, TP26, TP27, TP3, TP4, TP5, TP9: ~, TestPoint:TestPoint_Pad_1.0x1.0mm
- removed TP10, TP11, TP13, TP14, TP15, TP17, TP19, TP20, TP22, TP6, TP8: ~, TestPoint:TestPoint_Pad_1.5x1.5mm
- removed U1, U2, U5, U6: LM393BIDR, Package_SO:SOIC-8_3.9x4.9mm_P1.27mm
- removed U3: MCP1804T-C002I/OT, Package_TO_SOT_SMD:SOT-23-5
- removed U4: CD4002BM96, Package_SO:SOIC-14_3.9x8.7mm_P1.27mm
- removed U7, U8: TSB712AIDT, Package_SO:SOIC-8_5.3x5.3mm_P1.27mm
- added Q24: AO3400A, Package_TO_SOT_SMD:SOT-23, F.Cu at (1.96, 1.73)
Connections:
- J1 pad 1: unconnected-(J1-Pad1) -> /BSPD-FAULT-VCU
- J1 pad 10: unconnected-(J1-Pad10) -> /IMD-FAULT
- J1 pad 11: unconnected-(J1-Pad11) -> /BMS-FAULT-VCU-BUF
- J1 pad 12: unconnected-(J1-Pad12) -> /IMD-FAULT-VCU-BUF
- J1 pad 13: unconnected-(J1-Pad13) -> /BOTS-A
- J1 pad 14: unconnected-(J1-Pad14) -> /BOTS-B
- J1 pad 15: unconnected-(J1-Pad15) -> /CRASH-SW-A
- J1 pad 16: unconnected-(J1-Pad16) -> /BOTS-A
- J1 pad 2: unconnected-(J1-Pad2) -> /BYPASS-BTN
- J1 pad 3: unconnected-(J1-Pad3) -> /HVILS-A
- J1 pad 4: unconnected-(J1-Pad4) -> /CRASH-SW-A
- J1 pad 5: unconnected-(J1-Pad5) -> /BOTS-B
- J1 pad 6: unconnected-(J1-Pad6) -> /SD-POWER
- J1 pad 7: unconnected-(J1-Pad7) -> /SD-POWER
- J1 pad 8: unconnected-(J1-Pad8) -> GND
- J1 pad 9: unconnected-(J1-Pad9) -> /BMS-FAULT
- J2 pad 1: unconnected-(J2-Pad1) -> /TRACTIVE-FAN-ON
- J2 pad 10: unconnected-(J2-Pad10) -> /POS-AIRS-DEBUG
- J2 pad 11: unconnected-(J2-Pad11) -> /NEG-AIRS-DEBUG
- J2 pad 12: unconnected-(J2-Pad12) -> /TSSI-STATUS
- J2 pad 13: unconnected-(J2-Pad13) -> GND
- J2 pad 2: unconnected-(J2-Pad2) -> /ACCY-FAN-ON
- J2 pad 3: unconnected-(J2-Pad3) -> BATT+
- J2 pad 4: unconnected-(J2-Pad4) -> BATT+
- J2 pad 5: unconnected-(J2-Pad5) -> GND
- J2 pad 9: unconnected-(J2-Pad9) -> /PRECHARGE-DEBUG
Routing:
- net unconnected-(J1-Pad8): track 147.2 -> 0.00 mm
- net /BMS-FAULT-VCU-BUF: track 129.1 -> 0.00 mm, vias 1 -> 0
- net /ISENSE-EXT: track 123.1 -> 0.00 mm, vias 2 -> 0
- net /BMS-FAULT-VCU: track 121.6 -> 0.00 mm, vias 3 -> 0
- net /BSPD-FAULT-VCU-BUF: track 120.2 -> 0.00 mm, vias 1 -> 0
- net /IMD-FAULT-VCU: track 113.0 -> 0.00 mm, vias 3 -> 0
- net GND: track 109.4 -> 0.00 mm, vias 73 -> 0
- net /IMD-FAULT-VCU-BUF: track 101.1 -> 0.00 mm, vias 1 -> 0
- net unconnected-(J1-Pad16): track 75.2 -> 0.00 mm
- net 12V: track 60.9 -> 0.00 mm, vias 26 -> 0
- net /BOTS-A: track 57.5 -> 0.00 mm
- net /BSE: track 57.1 -> 0.00 mm, vias 1 -> 0
- net /IMD-FAULT: track 54.1 -> 0.00 mm, vias 1 -> 0
- net BATT+PROT: track 39.2 -> 0.00 mm, vias 18 -> 0
- net /BMS-FAULT: track 38.6 -> 0.00 mm, vias 1 -> 0
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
